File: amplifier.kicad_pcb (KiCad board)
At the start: 2 copper layers, 50 x 35 mm, 24 parts

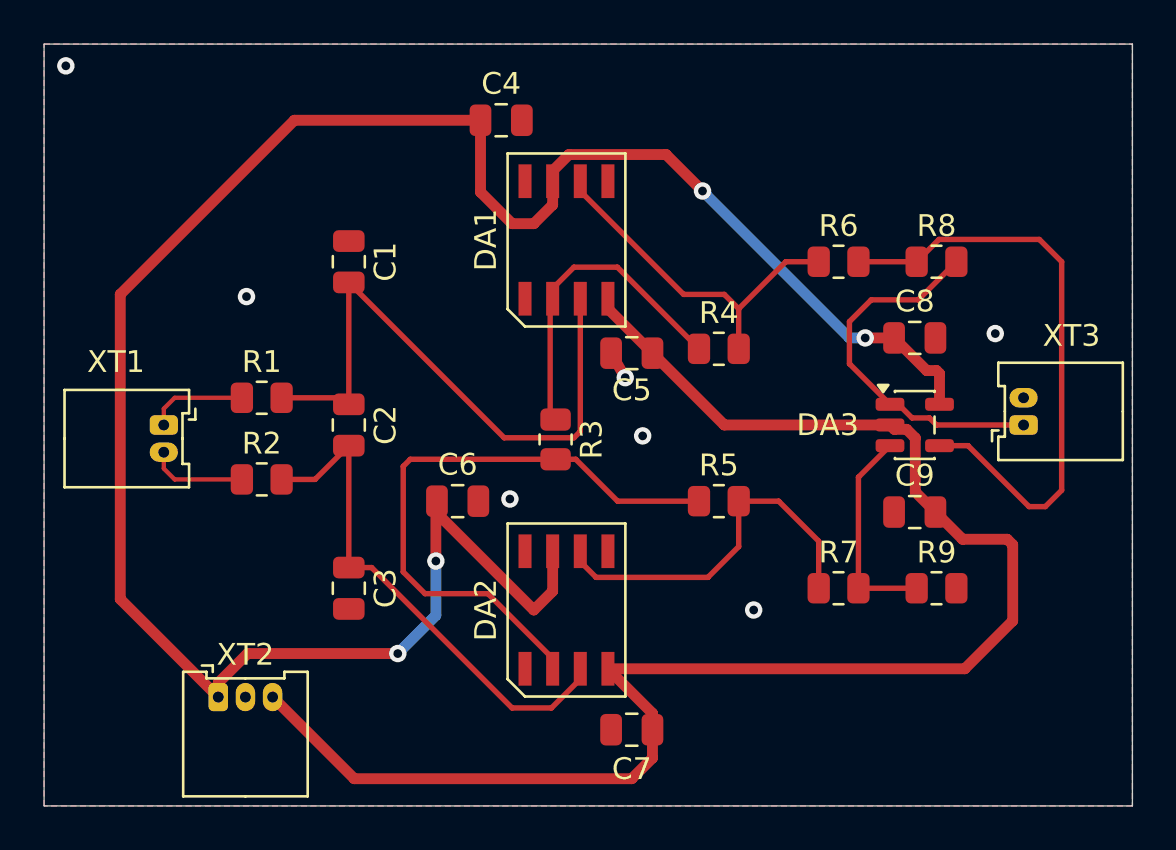
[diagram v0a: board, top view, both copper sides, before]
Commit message: УГО ОУ по ГОСТ 2.759, трассировка без острых и прямых углов
- library: ОУ с разделительными линиями доп. полей
- плата: изломы только 45°, новый переход у DA2.7, DRC 0/0/0
- обновлены docs, README, README.pdf

Co-Authored-By: Claude Opus 5.5 <noreply@anthropic.com>
Claude-Session: https://claude.ai/code/session_01Q3XDjd6y7RpdZFKAKCxfku
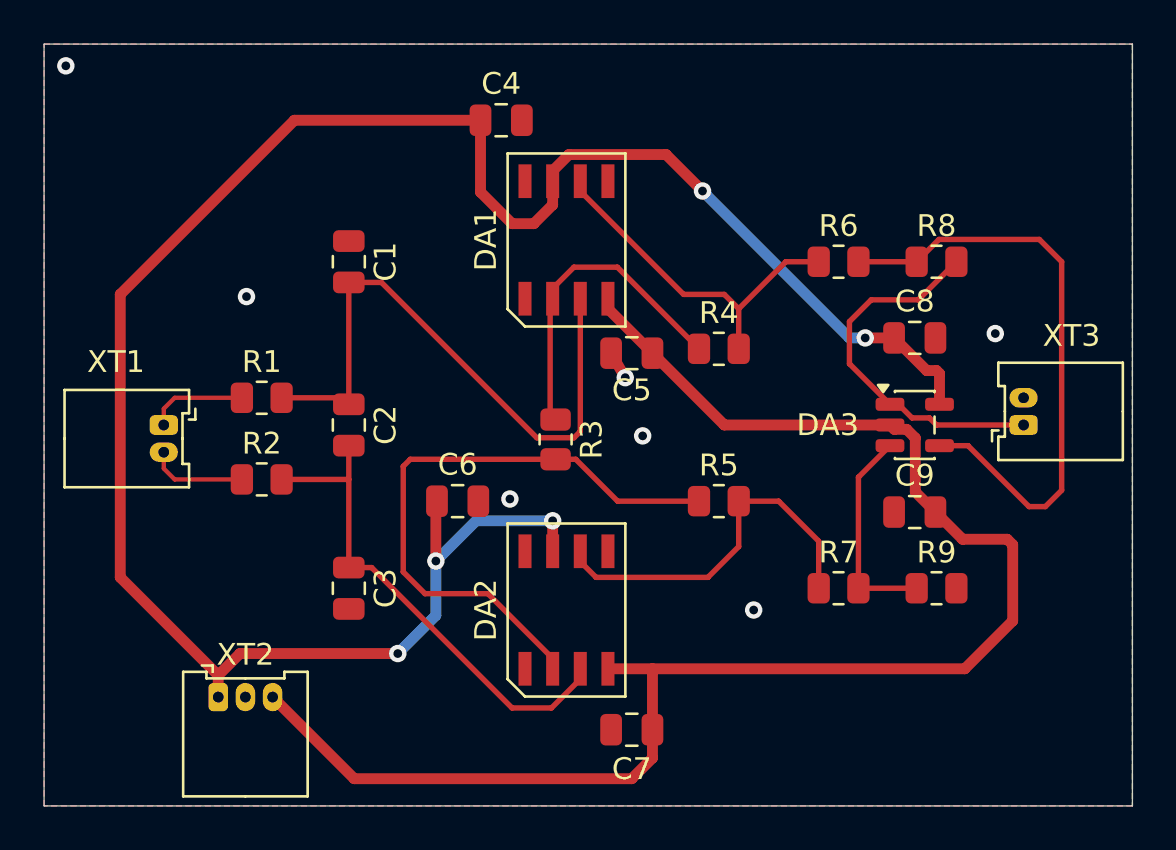
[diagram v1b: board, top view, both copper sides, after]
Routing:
- net +3V3: track 100.1 -> 96.9 mm, vias 4 -> 5
- net -3V3: track 72.3 -> 71.5 mm
- net Net-(DA2-+IN): track 23.7 -> 23.0 mm
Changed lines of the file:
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@@
 			)
 		)
-		(property "Manufacturer_Part_Number" ""
+		(property "Manufacturer_Part_Number" "CL21B123KBANNNC"
 			(at 0 0 270)
 			(unlocked yes)
@@
 			)
 		)
-		(property "Manufacturer_Part_Number" ""
+		(property "Manufacturer_Part_Number" "C0805C124K1RACTU"
 			(at 0 0 270)
 			(unlocked yes)
@@
 			)
 		)
-		(property "Manufacturer_Part_Number" ""
+		(property "Manufacturer_Part_Number" "CL21B123KBANNNC"
 			(at 0 0 270)
 			(unlocked yes)
@@
 	)
 	(segment
+		(start 122.638 88.0875)
+		(end 124.345 88.0875)
+		(width 0.25)
+		(layer "F.Cu")
+		(net "Net-(DA1-+IN)")
+	)
+	(segment
 		(start 124.635 87.7976)
 		(end 124.3451 88.0875)
@@
 	)
 	(segment
-		(start 110.9125 86.25)
-		(end 113.7 86.25)
+		(start 114 80.95)
+		(end 115.5 80.95)
 		(width 0.25)
 		(layer "F.Cu")
@@
 	)
 	(segment
-		(start 124.3451 88.0875)
-		(end 121.1375 88.0875)
+		(start 110.912 86.25)
+		(end 114 86.25)
 		(width 0.25)
 		(layer "F.Cu")
@@
 	)
 	(segment
-		(start 124.635 81.7)
-		(end 124.635 87.7976)
+		(start 115.5 80.95)
+		(end 122.638 88.0875)
 		(width 0.25)
 		(layer "F.Cu")
@@
 	)
 	(segment
-		(start 113.7 86.25)
-		(end 114 86.55)
+		(start 124.635 81.7)
+		(end 124.635 87.7976)
 		(width 0.25)
 		(layer "F.Cu")
@@
 	)
 	(segment
-		(start 121.1375 88.0875)
-		(end 114 80.95)
-		(width 0.25)
+		(start 127.95 101.5)
+		(end 127.95 98.7)
+		(width 0.5)
 		(layer "F.Cu")
-		(net "Net-(DA1-+IN)")
+		(net "-3V3")
 	)
 	(segment
@@
 	)
 	(segment
-		(start 127.95 100.745)
-		(end 125.905 98.7)
-		(width 0.5)
-		(layer "F.Cu")
-		(net "-3V3")
-	)
-	(segment
 		(start 144.5 96.5)
 		(end 144.5 93)
@@
 	)
 	(segment
-		(start 127.95 101.5)
-		(end 127.95 100.745)
-		(width 0.5)
-		(layer "F.Cu")
-		(net "-3V3")
-	)
-	(segment
 		(start 142.3 98.7)
 		(end 144.5 96.5)
@@
 	)
 	(segment
-		(start 118.05 91.55)
-		(end 122.5 96)
+		(start 108 100)
+		(end 108 99)
 		(width 0.5)
 		(layer "F.Cu")
@@
 	)
 	(segment
-		(start 118 93.75)
-		(end 118 91.05)
-		(width 0.5)
-		(layer "F.Cu")
-		(net "+3V3")
-	)
-	(segment
 		(start 124.115 75.075)
 		(end 128.575 75.075)
@@
 	)
 	(segment
-		(start 108 100)
-		(end 108 99.35)
-		(width 0.5)
-		(layer "F.Cu")
-		(net "+3V3")
-	)
-	(segment
-		(start 123.365 95.135)
-		(end 123.365 93.3)
-		(width 0.5)
-		(layer "F.Cu")
-		(net "+3V3")
-	)
-	(segment
 		(start 140.55 85)
 		(end 141 85)
@@
 	)
 	(segment
-		(start 118 91.05)
-		(end 118.05 91)
+		(start 123.365 91.9)
+		(end 123.365 93.3)
 		(width 0.5)
 		(layer "F.Cu")
@@
 	)
 	(segment
-		(start 122.5 96)
-		(end 123.365 95.135)
+		(start 108 99)
+		(end 103.5 94.5)
 		(width 0.5)
 		(layer "F.Cu")
@@
 	)
 	(segment
-		(start 108 100)
-		(end 103.5 95.5)
+		(start 108 99)
+		(end 109 98)
 		(width 0.5)
 		(layer "F.Cu")
@@
 	)
 	(segment
-		(start 103.5 95.5)
+		(start 103.5 94.5)
 		(end 103.5 81.5)
 		(width 0.5)
@@
 	)
 	(segment
-		(start 108 99.35)
-		(end 109.35 98)
+		(start 109 98)
+		(end 116.25 98)
 		(width 0.5)
 		(layer "F.Cu")
@@
 	)
 	(segment
-		(start 109.35 98)
-		(end 116.25 98)
-		(width 0.5)
-		(layer "F.Cu")
-		(net "+3V3")
-	)
-	(segment
-		(start 118.05 91)
-		(end 118.05 91.55)
+		(start 118 93.75)
+		(end 118 91)
 		(width 0.5)
 		(layer "F.Cu")
@@
 	)
 	(via
+		(at 123.365 91.9)
+		(size 0.8)
+		(drill 0.4)
+		(layers "F.Cu" "B.Cu")
+		(net "+3V3")
+	)
+	(via
 		(at 116.25 98)
 		(size 0.8)
@@
 	)
 	(segment
+		(start 118 93.75)
+		(end 119.85 91.9)
+		(width 0.5)
+		(layer "B.Cu")
+		(net "+3V3")
+	)
+	(segment
+		(start 119.85 91.9)
+		(end 123.365 91.9)
+		(width 0.5)
+		(layer "B.Cu")
+		(net "+3V3")
+	)
+	(segment
 		(start 126.05 84.2)
 		(end 126.7 85.326)
@@
 	)
 	(segment
-		(start 110.9125 90)
-		(end 112.45 90)
-		(width 0.25)
-		(layer "F.Cu")
-		(net "Net-(DA2-+IN)")
-	)
-	(segment
 		(start 114 94.05)
 		(end 115.05 94.05)
@@
 	)
 	(segment
-		(start 112.45 90)
-		(end 114 88.45)
-		(width 0.25)
-		(layer "F.Cu")
-		(net "Net-(DA2-+IN)")
-	)
-	(segment
 		(start 123.31 100.5)
 		(end 124.635 99.175)
@@
 	)
 	(segment
+		(start 110.912 90)
+		(end 114 90)
+		(width 0.25)
+		(layer "F.Cu")
+		(net "Net-(DA2-+IN)")
+	)
+	(segment
 		(start 114 88.45)
 		(end 114 94.05)
@@
 		(width 0.25)
 		(layer "F.Cu")
-		(net "Net-(DA3--IN)")
-	)
-	(segment
-		(start 140.0875 80)
-		(end 140.0875 80.1625)
-		(width 0.25)
-		(layer "F.Cu")
